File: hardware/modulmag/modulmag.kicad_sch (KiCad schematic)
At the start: 44 parts, among them J1 DEBUG, J2 BUS_IN, J3 BUS_OUT, J4 BŐVÍTŐ, U2 TCAN1044AVDRQ1, U3 ESD2CAN24-Q1, U5 AP2112K-3.3TRG1, U6 STM32F303RET6, Y1 8MHz

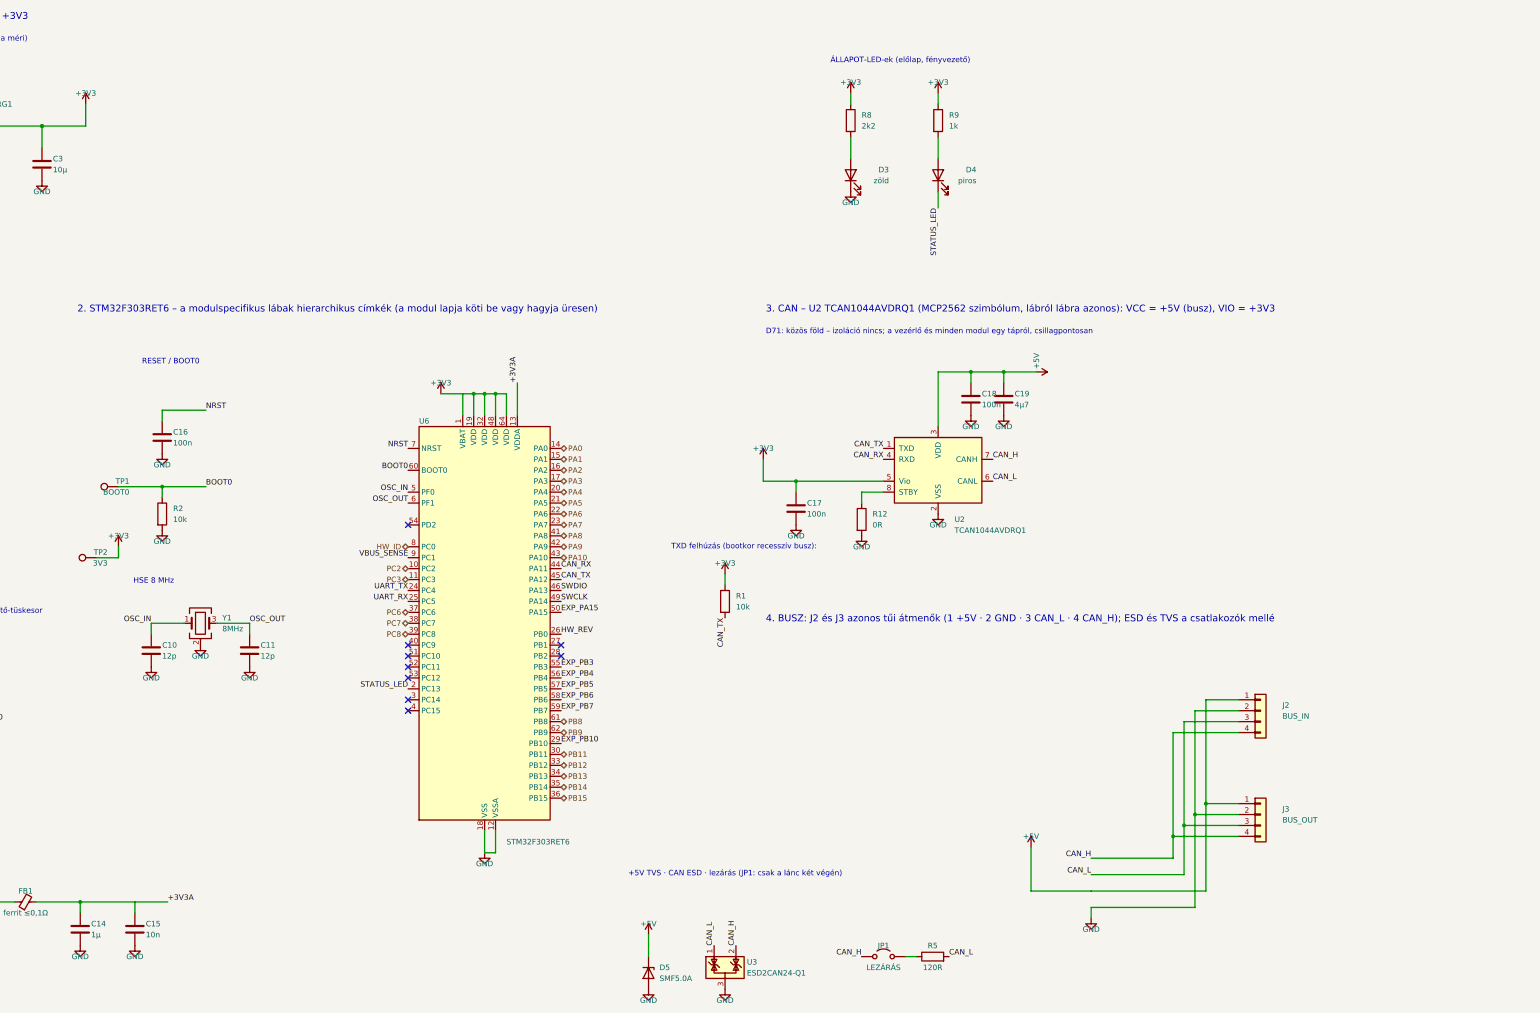
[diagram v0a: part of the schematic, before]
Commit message: Hardver: szakértői javítások (D74–D77), STM32L433 + SN65HVD230 + GND-ági polaritásvédelem (D78–D81), teljes ellenőrzés
- D74–D77: busz-GND ellenállás, CAN-fojtó-hely, TVS a +5V_BUCK-on és a VUSB-n, bemenetvédelem,
  230 V-os és antenna-tiltás a NYÁK-on, SCT-jack footprint
- D78–D80: modul-MCU STM32L433RCT3 (VIN_SENSE PB1, LED: TIM15/TIM16, I_SENSE PA3), modul-transceiver
  SN65HVD230, N-FET a GND-ágban (vezérlő Q1, LED Q201, relé Q100), MCP9701A, táp-LED a +5V-ról,
  2 oz a LED-/relémodulon, AP2112K marad; D81 javaslat (TPD4E02B04 a bemeneteken)
- CubeMX-projektek L433-ra, fejsoros kódgenerálással ellenőrizve (minden periféria inicializálódik)
- gen/ellenorzes.py (ERC, láb ↔ pad, modulmag, CubeMX, polaritásvédelem, NYÁK ↔ rajz, DRC) – 0 hiba
- gen/bom.sh + bom/*.csv darabjegyzék; docs/komponenslista.md a konzulensnek
- kontextus: DONTESEK D74–D81, specifikációk, ATTEKINTES, NAPLO, beszerzési lista; alkatrészkészlet-jegyzet (claude.ai)

Co-Authored-By: Claude Opus 5.5 <noreply@anthropic.com>
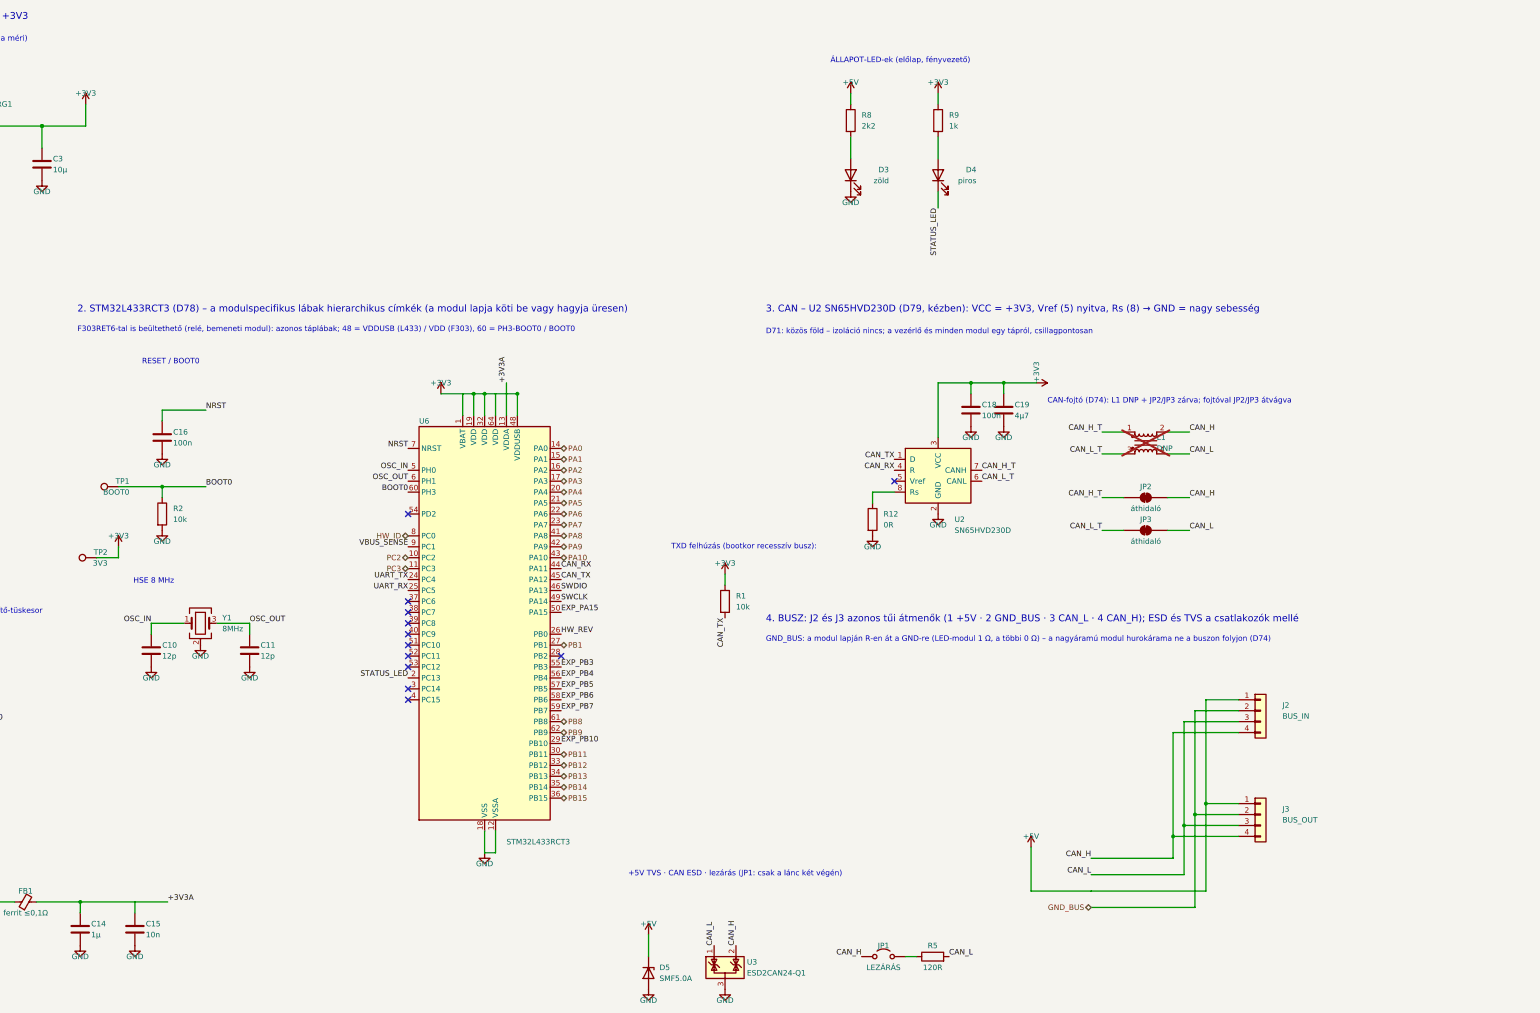
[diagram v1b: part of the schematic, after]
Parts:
- removed C17: 100n, Capacitor_SMD:C_0603_1608Metric, symbol Device:C
- removed U2: TCAN1044AVDRQ1, Package_SO:SOIC-8_3.9x4.9mm_P1.27mm, symbol Interface_CAN_LIN:MCP2562-E-SN
- removed U6: STM32F303RET6, Package_QFP:LQFP-64_10x10mm_P0.5mm, symbol MCU_ST_STM32F3:STM32F303RETx
- added JP2, JP3: áthidaló, Jumper:SolderJumper-2_P1.3mm_Bridged_RoundedPad1.0x1.5mm, symbol Jumper:SolderJumper_2_Bridged
- added L1: DNP, Inductor_SMD:L_CommonModeChoke_Coilank_ACM3225, symbol Device:Filter_EMI_CommonMode
- added U2: SN65HVD230D, Package_SO:SOIC-8_3.9x4.9mm_P1.27mm, symbol Interface_CAN_LIN:SN65HVD230
- added U6: STM32L433RCT3, Package_QFP:LQFP-64_10x10mm_P0.5mm, symbol MCU_ST_STM32L4:STM32L433RCTx
- D3: Megjegyzés táp-LED -> táp-LED: a busz 5 V-ja (HL-PST-1608U51GC, 522 nm)
- R12: Megjegyzés STB → normál mód (nyitva: készenlét) -> Rs → GND: nagy sebesség; 10–100 k: meredekség-szabályozás (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
- R8: Megjegyzés (none) -> D78: a +5V-ról – a kézben lévő zöld LED (522 nm) nyitófeszü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
- TP1: Megjegyzés 3V3-ra húzva: ROM-bootloader (USART1) -> 3V3-ra húzva: ROM-bootloader – a USART-jai nem a J1-en vann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
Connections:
- net +3V3: now also C18.1, C19.1, U2.3 (VCC), U6.1 (VBAT), U6.19 (VDD), U6.32 (VDD), U6.48 (VDDUSB), U6.64 (VDD); no longer R8.1
- net +3V3A: now also U6.13 (VDDA)
- net +5V: now also R8.1; no longer C18.1, C19.1
- net BOOT0: now also U6.60 (PH3)
- net CAN_H: now also JP2.2 (B), L1.2
- net CAN_L: now also JP3.2 (B), L1.4
- net CAN_RX: now also U2.4 (R), U6.44 (PA11)
- net CAN_TX: now also U2.1 (D), U6.45 (PA12)
- net EXP_PA15: now also U6.50 (PA15)
- net EXP_PB10: now also U6.29 (PB10)
- net EXP_PB3: now also U6.55 (PB3)
- net EXP_PB4: now also U6.56 (PB4)
- net EXP_PB5: now also U6.57 (PB5)
- net EXP_PB6: now also U6.58 (PB6)
- net EXP_PB7: now also U6.59 (PB7)
- net GND: now also U2.2 (GND), U6.12 (VSSA), U6.18 (VSS), U6.31 (VSS), U6.47 (VSS), U6.63 (VSS); no longer J2.2 (Pin_2), J3.2 (Pin_2)
- net HW_ID: now also U6.8 (PC0)
- net HW_REV: now also U6.26 (PB0)
- net NRST: now also U6.7 (NRST)
- net OSC_IN: now also U6.5 (PH0)
- net OSC_OUT: now also U6.6 (PH1)
- net PA0: now also U6.14 (PA0)
- net PA1: now also U6.15 (PA1)
- net PA10: now also U6.43 (PA10)
- net PA2: now also U6.16 (PA2)
- net PA3: now also U6.17 (PA3)
- net PA4: now also U6.20 (PA4)
- net PA5: now also U6.21 (PA5)
- net PA6: now also U6.22 (PA6)
- net PA7: now also U6.23 (PA7)
- net PA8: now also U6.41 (PA8)
- net PA9: now also U6.42 (PA9)
- net PB11: now also U6.30 (PB11)
- net PB12: now also U6.33 (PB12)
- net PB13: now also U6.34 (PB13)
- net PB14: now also U6.35 (PB14)
- net PB15: now also U6.36 (PB15)
- net PB8: now also U6.61 (PB8)
- net PB9: now also U6.62 (PB9)
- net PC2: now also U6.10 (PC2)
- net PC3: now also U6.11 (PC3)
- net STATUS_LED: now also U6.2 (PC13)
- net SWCLK: now also U6.49 (PA14)
- net SWDIO: now also U6.46 (PA13)
- net UART_RX: now also U6.25 (PC5)
- net UART_TX: now also U6.24 (PC4)
- net VBUS_SENSE: now also U6.9 (PC1)
- net at R12.1: now also U2.8 (Rs)
- new net CAN_H_T: JP2.1 (A), L1.1, U2.7 (CANH)
- new net CAN_L_T: JP3.1 (A), L1.3, U2.6 (CANL)
- new net GND_BUS: J2.2 (Pin_2), J3.2 (Pin_2)
- new net PB1: U6.27 (PB1)
- no-connect marks 10 -> 13
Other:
- note added: "2. STM32L433RCT3 (D78) – a modulspecifikus lábak hierarchikus címkék (a modul lapja köti be vagy hagyja üresen)"
- note added: "3. CAN – U2 SN65HVD230D (D79, kézben): VCC = +3V3, Vref (5) nyitva, Rs (8) → GND = nagy sebesség"
- note added: "4. BUSZ: J2 és J3 azonos tűi átmenők (1 +5V · 2 GND_BUS · 3 CAN_L · 4 CAN_H); ESD és TVS a csatlakozók mellé"
- note added: "CAN-fojtó (D74): L1 DNP + JP2/JP3 zárva; fojtóval JP2/JP3 átvágva"
- note added: "F303RET6-tal is beültethető (relé, bemeneti modul): azonos táplábak; 48 = VDDUSB (L433) / VDD (F303), 60 = PH3-BOOT0 / BOOT0"
- note added: "GND_BUS: a modul lapján R-en át a GND-re (LED-modul 1 Ω, a többi 0 Ω) – a nagyáramú modul hurokárama ne a buszon folyjon (D74)"
- note removed: "2. STM32F303RET6 – a modulspecifikus lábak hierarchikus címkék (a modul lapja köti be vagy hagyja üresen)"
- note removed: "3. CAN – U2 TCAN1044AVDRQ1 (MCP2562 szimbólum, lábról lábra azonos): VCC = +5V (busz), VIO = +3V3"
- note removed: "4. BUSZ: J2 és J3 azonos tűi átmenők (1 +5V · 2 GND · 3 CAN_L · 4 CAN_H); ESD és TVS a csatlakozók mellé"
- title: Modulmag – STM32F303RET6, CAN, táp a buszról (+5V → 3,3 V) -> Modulmag – STM32L433RCT3, CAN, táp a buszról (+5V → 3,3 V)

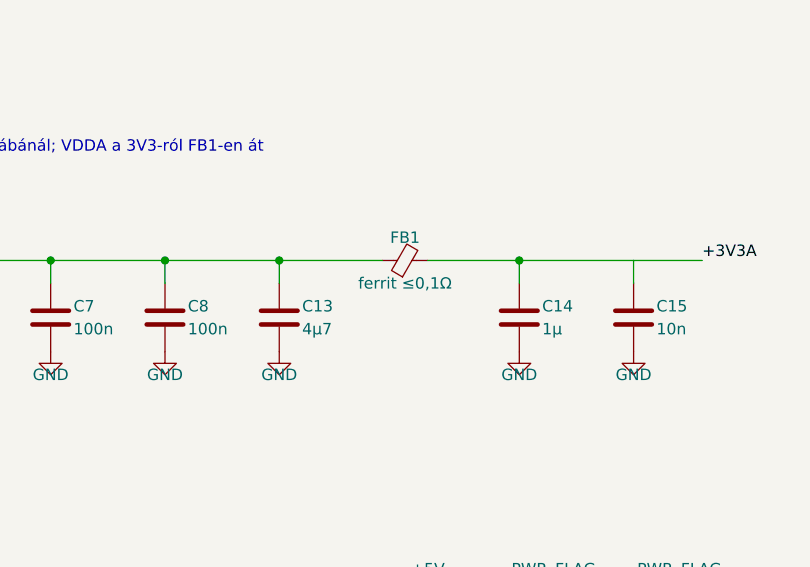
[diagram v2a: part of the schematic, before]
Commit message: Hardver: legolcsóbb beszerzés (D84) – Hestore + DigiKey, a rajz a kapható típusokra igazítva; beszerzési lista
- gen/beszerzes.py → bom/beszerzes.csv: BOM-tételenként forrás, Hestore-kód, nettó ár, készlet
- J1/J100 Degson DG250, J201 DG128 (15 A), J202–J204 KF128, F201 15 A; L1/L3 HPI0630 (saját footprint);
  R209 CRE2512; C40/C41 12 pF; ESP32-C6-WROOM-1-N8; SS56C, BAT54HT1G, STPS3L60U, BLM18EG221
- NYÁK-ok újragenerálva (a layout még nem indult el); bekötés változatlan, ellenorzes.py: 0 hiba
- SAMPLE-KERESEK: az NTMFS5C604NL nincs kézben (javítva)

Co-Authored-By: Claude Opus 5.5 <noreply@anthropic.com>
Claude-Session: https://claude.ai/code/session_01KVtZMUPbtveTXy9VyJshyt
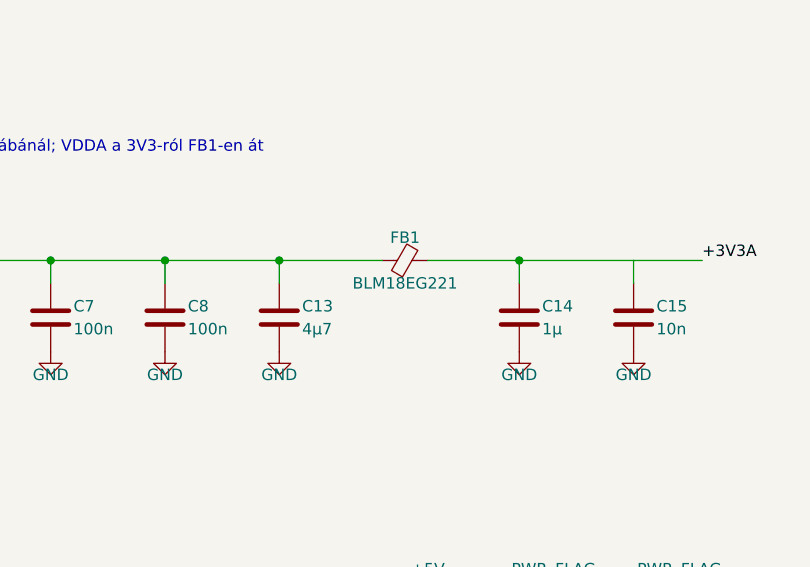
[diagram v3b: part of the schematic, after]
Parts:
- FB1: value ferrit ≤0,1Ω -> BLM18EG221; Megjegyzés vagy 0 Ω -> D84: Murata BLM18EG221TN1D (0,15 Ω – a VDDA pár mA-jén elha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
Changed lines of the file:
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@@
 			)
 		)
-		(property "Value" "ferrit ≤0,1Ω"
+		(property "Value" "BLM18EG221"
 			(at 107.95 227.33 90)
 			(show_name no)
@@
 			)
 		)
-		(property "Megjegyzés" "vagy 0 Ω"
+		(property "Megjegyzés" "D84: Murata BLM18EG221TN1D (0,15 Ω – a VDDA pár mA-jén elhanyagolható); vagy 0 Ω"
 			(at 107.95 224.79 90)
 			(hide yes)

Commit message: Hardver: legolcsóbb beszerzés LCSC-ről (D85), megszűnt FET-ek pótlása, LCSC-kosárlista
- gen/lcsc.py: LCSC-árak a JLC alkatrészkeresőjéből; gen/beszerzes.py soronként a legolcsóbb forrás (Hestore / LCSC, ÁFA-val)
- bom/lcsc-kosar.csv: 99 tétel (~15 eFt), az LCSC BOM Tooljába feltölthető; házak később, ST-Link/Nucleo kézben
- Q202–Q207 NTD5C648NL → NCE6080K, Q201 NTMFS5C604NL → NCEP6090AGU (nem kaphatók), F201 → NANO² 15 A,
  D211–D216 SS56B, J1/J100 DG128, L1/L3 LCSC-s 0630-as tekercs, kis ESR-ű kvarcok
- bekötés változatlan (netlista 0 / 0), ellenorzes.py: 0 hiba

Co-Authored-By: Claude Opus 5.5 <noreply@anthropic.com>
Claude-Session: https://claude.ai/code/session_01KVtZMUPbtveTXy9VyJshyt
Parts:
- Y1: Megjegyzés (none) -> D85: 3TJ480000JWLAC (LCSC C3031779) – CL = 10 pF, ESR ≤ 120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
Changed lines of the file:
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@@
+			)
+		)
+		(property "Megjegyzés" "D85: 3TJ480000JWLAC (LCSC C3031779) – CL = 10 pF, ESR ≤ 120 Ω (HSE gm-tartalék ~7)"
+			(at 148.59 160.02 0)
+			(hide yes)
+			(show_name no)
+			(do_not_autoplace no)
+			(effects
+				(font
+					(size 1.27 1.27)
+				)
 			)
 		)

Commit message: Hardver: kézzel átrendezett kapcsolási rajzok (D67), védelem a generátor felülírása ellen; rajzdátum 10-23
- mind az öt lap kézi szerkesztésű – gen/kezi-lapok.txt; a build.sh ezeket nem generálja újra, csak ellenőrzi (felülírás: --force)
- bekötés változatlan (netlista 0 / 0), ERC rendben, ellenorzes.py: 0 hiba
- komponenslista: állapot 10-23

Co-Authored-By: Claude Opus 5.5 <noreply@anthropic.com>
Claude-Session: https://claude.ai/code/session_01KVtZMUPbtveTXy9VyJshyt
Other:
- note removed: "Generálva a MODULMAG-SPEC.md alapján (hardware/gen/modulmag.py) – kézi szerkesztés helyett a generátort módosítsd."
- moved on the sheet: C9, R1
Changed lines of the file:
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@@
 	(title_block
 		(title "Modulmag – STM32L433RCT3, CAN, táp a buszról (+5V → 3,3 V)")
-		(date "2026-10-20")
+		(date "2026-10-23")
 		(rev "v1 vázlat")
 		(company "Moduláris okosotthon platform – szakdolgozat")
@@
 	(text "TXD felhúzás (bootkor recesszív busz):"
 		(exclude_from_sim no)
-		(at 258 143 0)
+		(at 310.07 187.45 0)
 		(effects
 			(font
@@
 		)
 	)
-	(text "Generálva a MODULMAG-SPEC.md alapján (hardware/gen/modulmag.py) – kézi szerkesztés helyett a generátort módosítsd."
-		(exclude_from_sim no)
-		(at 20 281 0)
-		(effects
-			(font
-				(size 1.3 1.3)
-			)
-			(justify left bottom)
-		)
-	)
 	(text "GND_BUS: a modul lapján R-en át a GND-re (LED-modul 1 Ω, a többi 0 Ω) – a nagyáramú modul hurokárama ne a buszon folyjon (D74)"
 		(exclude_from_sim no)
-		(at 280 164.5 0)
+		(at 256.54 174.68 0)
 		(effects
 			(font
@@
 	(text "4. BUSZ: J2 és J3 azonos tűi átmenők (1 +5V · 2 GND_BUS · 3 CAN_L · 4 CAN_H); ESD és TVS a csatlakozók mellé"
 		(exclude_from_sim no)
-		(at 280 160 0)
+		(at 256.54 170.18 0)
 		(effects
 			(font
@@
 	)
 	(junction
-		(at 64.77 59.69)
+		(at 68.58 59.69)
 		(diameter 0)
 		(color 0 0 0 0)
@@
 	)
 	(junction
-		(at 222.25 106.68)
-		(diameter 0)
-		(color 0 0 0 0)
-	)
-	(junction
-		(at 111.76 44.45)
-		(diameter 0)
-		(color 0 0 0 0)
-	)
-	(junction
 		(at 120.65 224.79)
 		(diameter 0)
@@
 	(wire
 		(pts
-			(xy 382.27 222.25) (xy 355.6 222.25)
-		)
-		(stroke
-			(width 0)
-			(type default)
-		)
-	)
-	(wire
-		(pts
 			(xy 57.15 116.84) (xy 57.15 111.76)
 		)
@@
 	(wire
 		(pts
-			(xy 355.6 222.25) (xy 341.63 222.25)
+			(xy 341.63 222.25) (xy 382.27 222.25)
 		)
 		(stroke
@@
 	(wire
 		(pts
-			(xy 64.77 121.92) (xy 57.15 121.92)
-		)
-		(stroke
-			(width 0)
-			(type default)
-		)
-	)
-	(wire
-		(pts
 			(xy 219.71 111.76) (xy 219.71 104.14)
 		)
@@
 	(wire
 		(pts
-			(xy 64.77 59.69) (xy 71.12 59.69)
-		)
-		(stroke
-			(width 0)
-			(type default)
-		)
-	)
-	(wire
-		(pts
 			(xy 111.76 44.45) (xy 121.92 44.45)
 		)
@@
 	(wire
 		(pts
-			(xy 57.15 121.92) (xy 39.37 121.92)
+			(xy 39.37 121.92) (xy 64.77 121.92)
 		)
 		(stroke
@@
 	(wire
 		(pts
-			(xy 270.51 148.59) (xy 270.51 151.13)
+			(xy 322.58 193.04) (xy 322.58 195.58)
 		)
 		(stroke
@@
 	(wire
 		(pts
-			(xy 55.88 59.69) (xy 64.77 59.69)
+			(xy 55.88 59.69) (xy 71.12 59.69)
 		)
 		(stroke
@@
 	(wire
 		(pts
-			(xy 64.77 59.69) (xy 64.77 62.23)
+			(xy 68.58 59.69) (xy 68.58 62.23)
 		)
 		(stroke
@@
 	)
 	(label "CAN_TX"
-		(at 270.51 158.75 270)
+		(at 322.58 203.2 270)
 		(effects
 			(font
@@
 	(symbol
 		(lib_id "power:GND")
-		(at 64.77 69.85 0)
+		(at 68.58 69.85 0)
 		(unit 1)
 		(body_style 1)
@@
 		(dnp no)
 		(property "Reference" "#PWR004"
-			(at 64.77 67.31 0)
+			(at 68.58 67.31 0)
 			(hide yes)
 			(show_name no)
@@
 		)
 		(property "Value" "GND"
-			(at 64.77 72.39 0)
+			(at 68.58 72.39 0)
 			(show_name no)
 			(do_not_autoplace no)
@@
 		)
 		(property "Footprint" ""
-			(at 64.77 69.85 0)
+			(at 68.58 69.85 0)
 			(hide yes)
 			(show_name no)
@@
 		)
 		(property "Datasheet" ""
-			(at 64.77 69.85 0)
+			(at 68.58 69.85 0)
 			(hide yes)
 			(show_name no)
@@
 		)
 		(property "Description" ""
-			(at 64.77 69.85 0)
+			(at 68.58 69.85 0)
 			(show_name no)
 			(do_not_autoplace no)
@@
 	(symbol
 		(lib_id "Device:R")
-		(at 270.51 154.94 0)
+		(at 322.58 199.39 0)
 		(unit 1)
 		(body_style 1)
@@
 		(dnp no)
 		(property "Reference" "R1"
-			(at 273.05 153.67 0)
+			(at 325.12 198.12 0)
 			(show_name no)
 			(do_not_autoplace no)
@@
 		)
 		(property "Value" "10k"
-			(at 273.05 156.21 0)
+			(at 325.12 200.66 0)
 			(show_name no)
 			(do_not_autoplace no)
@@
 		)
 		(property "Footprint" "Resistor_SMD:R_0603_1608Metric"
-			(at 270.51 154.94 0)
+			(at 322.58 199.39 0)
 			(hide yes)
 			(show_name no)
@@
 		)
 		(property "Datasheet" ""
-			(at 270.51 154.94 0)
+			(at 322.58 199.39 0)
 			(hide yes)
 			(show_name no)
@@
 		)
 		(property "Description" ""
-			(at 270.51 154.94 0)
+			(at 322.58 199.39 0)
 			(show_name no)
 			(do_not_autoplace no)
@@
 	(symbol
 		(lib_id "power:+3V3")
-		(at 270.51 148.59 0)
+		(at 322.58 193.04 0)
 		(unit 1)
 		(body_style 1)
@@
 		(dnp no)
 		(property "Reference" "#PWR041"
-			(at 270.51 146.05 0)
+			(at 322.58 190.5 0)
 			(hide yes)
 			(show_name no)
@@
 		)
 		(property "Value" "+3V3"
-			(at 270.51 146.05 0)
+			(at 322.58 190.5 0)
 			(show_name no)
 			(do_not_autoplace no)
@@
 		)
 		(property "Footprint" ""
-			(at 270.51 148.59 0)
+			(at 322.58 193.04 0)
 			(hide yes)
 			(show_name no)
@@
 		)
 		(property "Datasheet" ""
-			(at 270.51 148.59 0)
+			(at 322.58 193.04 0)
 			(hide yes)
 			(show_name no)
@@
 		)
 		(property "Description" ""
-			(at 270.51 148.59 0)
+			(at 322.58 193.04 0)
 			(show_name no)
 			(do_not_autoplace no)
@@
 	(symbol
 		(lib_id "Device:C")
-		(at 64.77 66.04 0)
+		(at 68.58 66.04 0)
 		(unit 1)
 		(body_style 1)
@@
 		(dnp no)
 		(property "Reference" "C9"
-			(at 67.31 64.77 0)
+			(at 71.12 64.77 0)
 			(show_name no)
 			(do_not_autoplace no)
@@
 		)
 		(property "Value" "100n"
-			(at 67.31 67.31 0)
+			(at 71.12 67.31 0)
 			(show_name no)
 			(do_not_autoplace no)
@@
 		)
 		(property "Footprint" "Capacitor_SMD:C_0603_1608Metric"
-			(at 64.77 66.04 0)
+			(at 68.58 66.04 0)
 			(hide yes)
 			(show_name no)
@@
 		)
 		(property "Datasheet" ""
-			(at 64.77 66.04 0)
+			(at 68.58 66.04 0)
 			(hide yes)
 			(show_name no)
@@
 		)
 		(property "Description" ""
-			(at 64.77 66.04 0)
+			(at 68.58 66.04 0)
 			(show_name no)
 			(do_not_autoplace no)
